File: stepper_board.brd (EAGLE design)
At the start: 101.1 x 81.3 mm, 83 parts

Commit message: Changed value of motor blocking cap
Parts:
- C7: value 100uF -> 330uF
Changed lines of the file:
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@@
 <?xml version="1.0" encoding="utf-8"?>
 <!DOCTYPE eagle SYSTEM "eagle.dtd">
-<eagle version="7.7.0">
+<eagle version="6.6.0">
 <drawing>
 <settings>
@@
 <pass name="Default">
 <param name="RoutingGrid" value="50mil"/>
-<param name="AutoGrid" value="1"/>
-<param name="Efforts" value="0"/>
-<param name="TopRouterVariant" value="1"/>
 <param name="tpViaShape" value="round"/>
 <param name="PrefDir.1" value="|"/>
@@
 <attribute name="VALUE" x="91.44" y="25.4" size="1.27" layer="27" rot="R180"/>
 </element>
-<element name="C7" library="rcl" package="UD-10X10_NICHICON" value="100uF" x="61.087" y="7.62" smashed="yes">
+<element name="C7" library="rcl" package="UD-10X10_NICHICON" value="330uF" x="61.087" y="7.62" smashed="yes">
 <attribute name="NAME" x="60.579" y="0.889" size="0.8128" layer="25" font="vector"/>
 <attribute name="VALUE" x="56.007" y="1.27" size="1.016" layer="27"/>

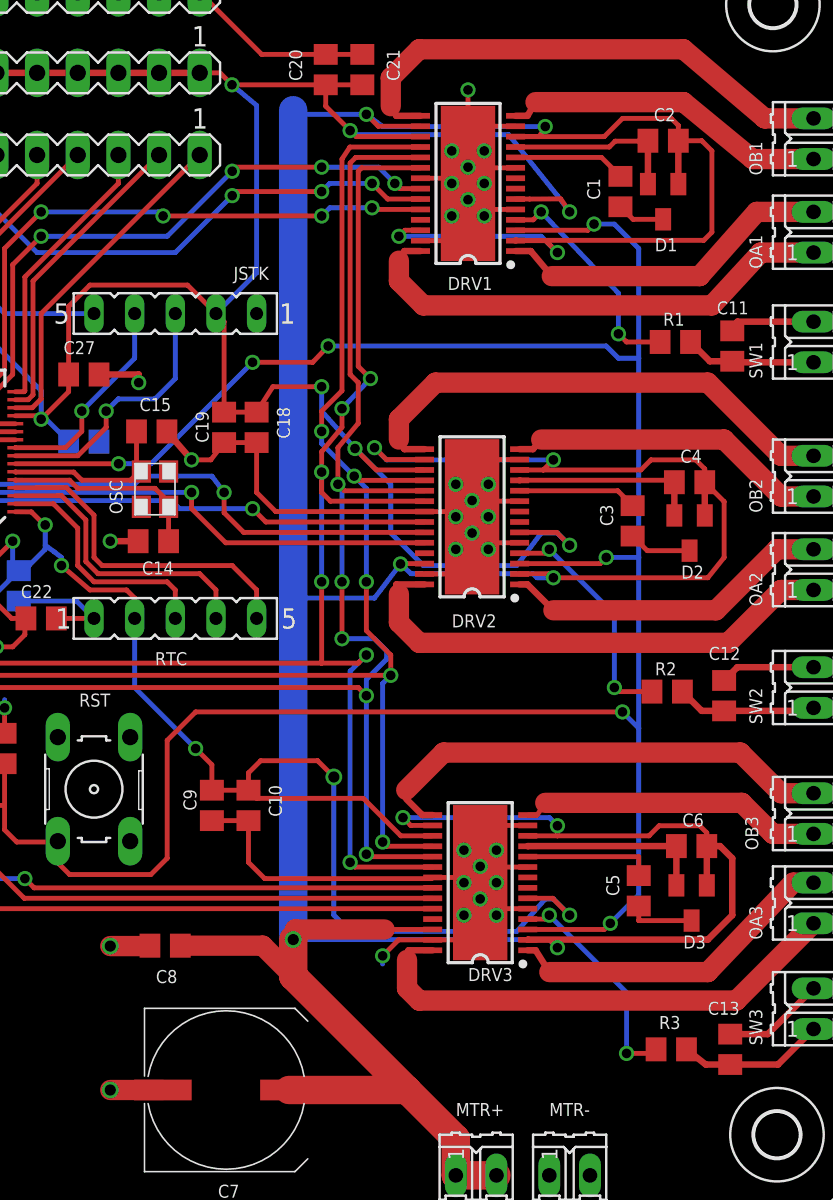
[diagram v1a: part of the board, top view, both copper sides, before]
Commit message: Made the power traces on the drivers slightly bigger
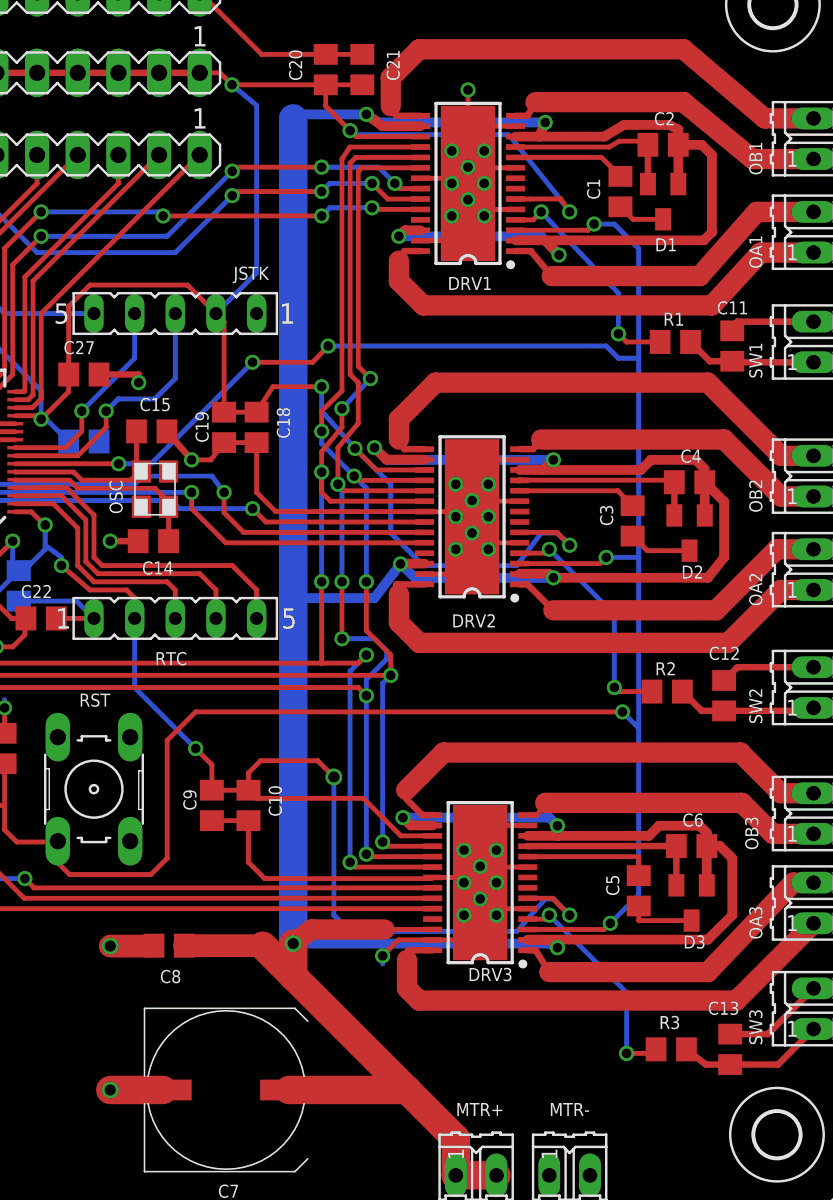
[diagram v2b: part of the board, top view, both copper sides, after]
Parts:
- moved C2 0.25 mm to (88.4, 66.7)
- moved C8 0.25 mm to (57.5, 16.6)
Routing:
- net VCC: track 302.7 -> 301.1 mm

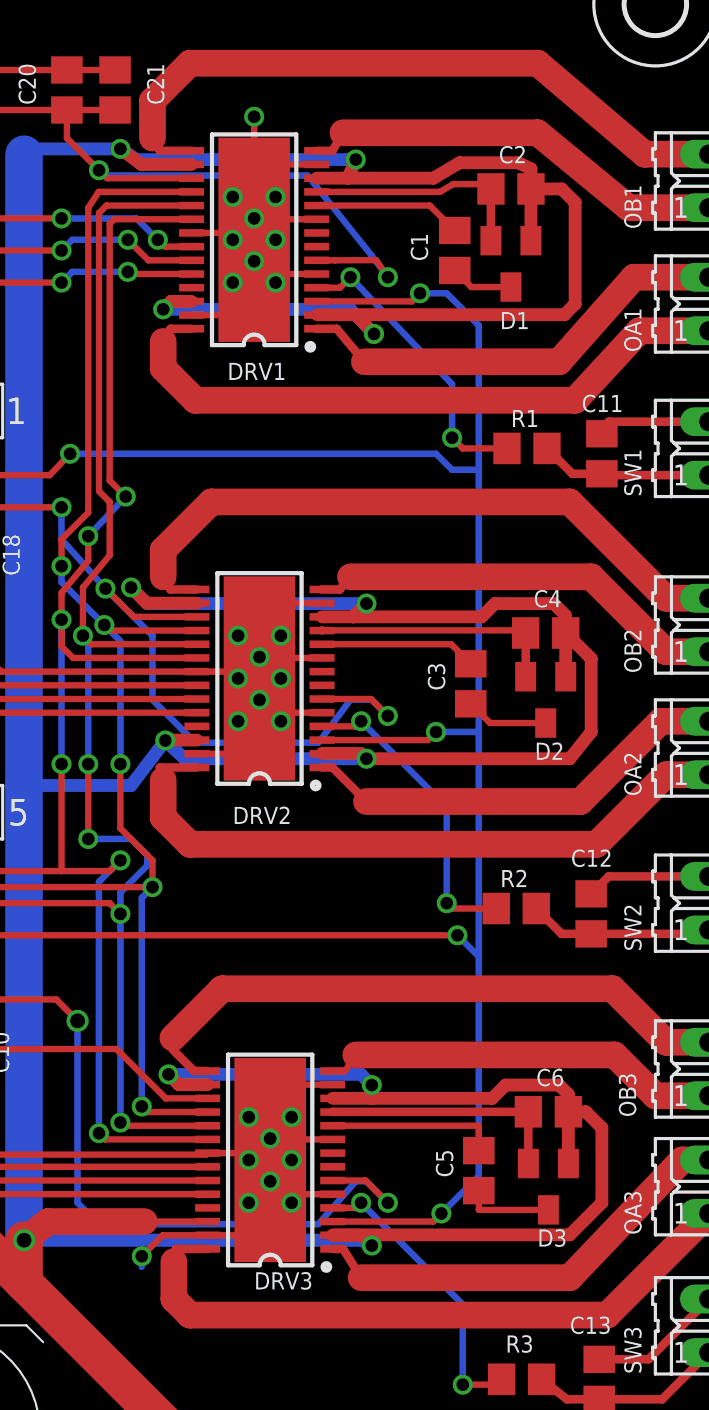
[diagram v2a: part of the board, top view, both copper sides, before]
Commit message: More tracing beefyness
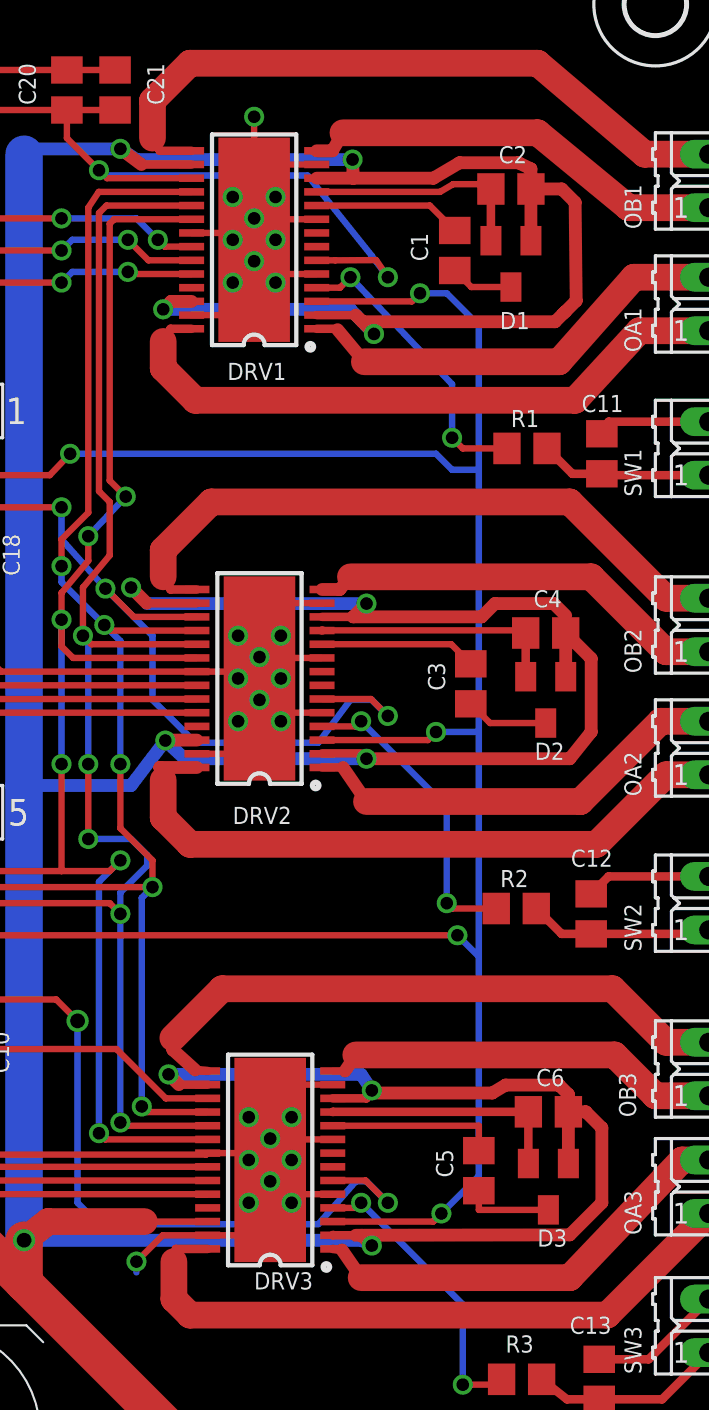
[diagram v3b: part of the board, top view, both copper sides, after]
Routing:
- net VCC: track 301.1 -> 296.3 mm
